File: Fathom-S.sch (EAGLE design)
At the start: 109 parts, among them IC1 LMH6643, IC2 LMH6643, IC3 ST490AB, IC4 ST490AB, IC5 FT230XS, Q1 BC817-40W, U1 MC7812, U2 MC7805, U4 INA139, U5 MC7805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

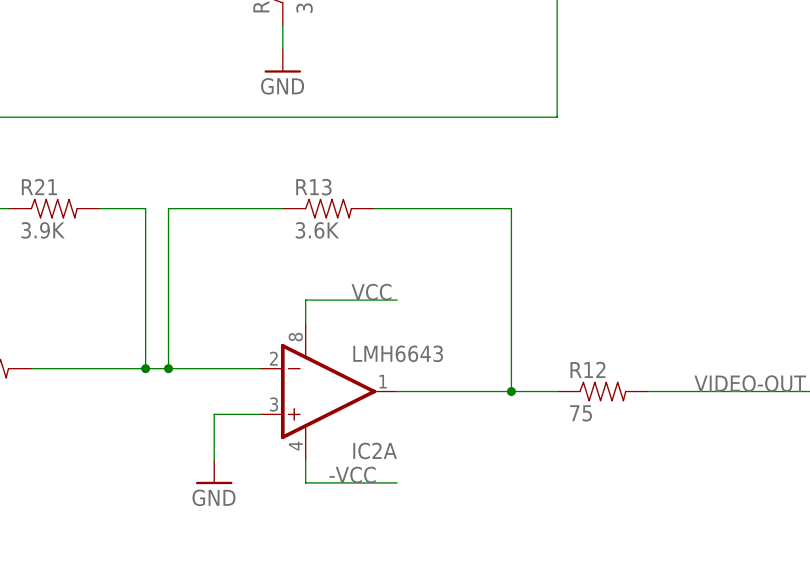
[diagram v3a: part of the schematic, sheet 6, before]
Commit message: Changed the op-amp package because the MSOPs are much cheaper for some reason.
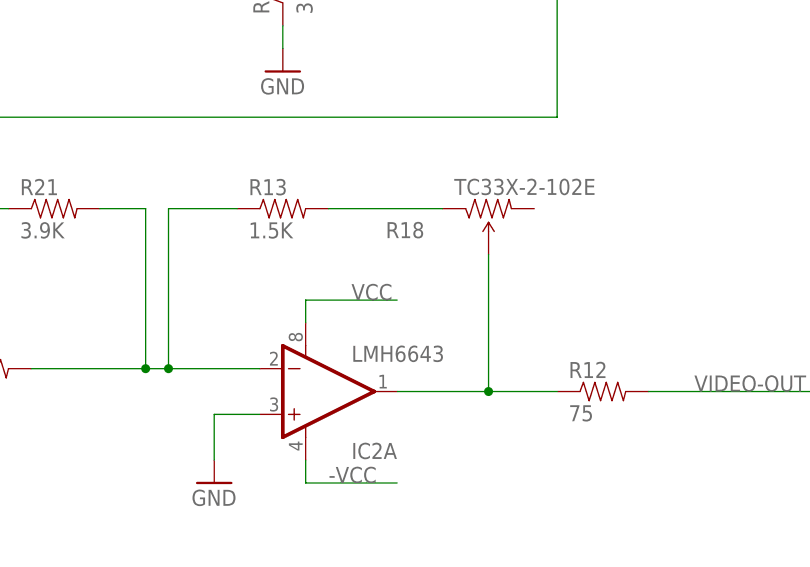
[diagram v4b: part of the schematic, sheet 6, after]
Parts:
- added R18: TC33X-2-102E, SparkFun-Electromechanical:TRIMPOT-2
- IC1, IC2: device SparkFun-AnalogIC:OPAMP-DUALU -> BlueRobotics-Main:OPAMP-DUALMSOP
- R13: value 3.6K -> 1.5K
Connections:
- new net N$12: R13.2, R18.CCW
- net N$17: now also R18.WIPER; no longer R13.2
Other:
- moved on the sheet: R13
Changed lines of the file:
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@@
 <grid distance="0.1" unitdist="inch" unit="inch" style="lines" multiple="1" display="no" altdistance="0.01" altunitdist="inch" altunit="inch"/>
 <layers>
-<layer number="1" name="Top" color="4" fill="1" visible="no" active="no"/>
-<layer number="2" name="Route2" color="1" fill="3" visible="no" active="no"/>
-<layer number="3" name="Route3" color="4" fill="3" visible="no" active="no"/>
-<layer number="14" name="Route14" color="1" fill="6" visible="no" active="no"/>
-<layer number="15" name="Route15" color="4" fill="6" visible="no" active="no"/>
-<layer number="16" name="Bottom" color="1" fill="1" visible="no" active="no"/>
-<layer number="17" name="Pads" color="2" fill="1" visible="no" active="no"/>
-<layer number="18" name="Vias" color="2" fill="1" visible="no" active="no"/>
-<layer number="19" name="Unrouted" color="6" fill="1" visible="no" active="no"/>
-<layer number="20" name="Dimension" color="15" fill="1" visible="no" active="no"/>
-<layer number="21" name="tPlace" color="7" fill="1" visible="no" active="no"/>
-<layer number="22" name="bPlace" color="7" fill="1" visible="no" active="no"/>
-<layer number="23" name="tOrigins" color="15" fill="1" visible="no" active="no"/>
-<layer number="24" name="bOrigins" color="15" fill="1" visible="no" active="no"/>
-<layer number="25" name="tNames" color="7" fill="1" visible="no" active="no"/>
-<layer number="26" name="bNames" color="7" fill="1" visible="no" active="no"/>
-<layer number="27" name="tValues" color="7" fill="1" visible="no" active="no"/>
-<layer number="28" name="bValues" color="7" fill="1" visible="no" active="no"/>
+<layer number="1" name="Top" color="4" fill="1" visible="yes" active="no"/>
+<layer number="2" name="Route2" color="1" fill="3" visible="yes" active="no"/>
+<layer number="3" name="Route3" color="4" fill="3" visible="yes" active="no"/>
+<layer number="14" name="Route14" color="1" fill="6" visible="yes" active="no"/>
+<layer number="15" name="Route15" color="4" fill="6" visible="yes" active="no"/>
+<layer number="16" name="Bottom" color="1" fill="1" visible="yes" active="no"/>
+<layer number="17" name="Pads" color="2" fill="1" visible="yes" active="no"/>
+<layer number="18" name="Vias" color="2" fill="1" visible="yes" active="no"/>
+<layer number="19" name="Unrouted" color="6" fill="1" visible="yes" active="no"/>
+<layer number="20" name="Dimension" color="15" fill="1" visible="yes" active="no"/>
+<layer number="21" name="tPlace" color="7" fill="1" visible="yes" active="no"/>
+<layer number="22" name="bPlace" color="7" fill="1" visible="yes" active="no"/>
+<layer number="23" name="tOrigins" color="15" fill="1" visible="yes" active="no"/>
+<layer number="24" name="bOrigins" color="15" fill="1" visible="yes" active="no"/>
+<layer number="25" name="tNames" color="7" fill="1" visible="yes" active="no"/>
+<layer number="26" name="bNames" color="7" fill="1" visible="yes" active="no"/>
+<layer number="27" name="tValues" color="7" fill="1" visible="yes" active="no"/>
+<layer number="28" name="bValues" color="7" fill="1" visible="yes" active="no"/>
 <layer number="29" name="tStop" color="7" fill="3" visible="no" active="no"/>
 <layer number="30" name="bStop" color="7" fill="6" visible="no" active="no"/>
@@
 <layer number="35" name="tGlue" color="7" fill="4" visible="no" active="no"/>
 <layer number="36" name="bGlue" color="7" fill="5" visible="no" active="no"/>
-<layer number="37" name="tTest" color="7" fill="1" visible="no" active="no"/>
-<layer number="38" name="bTest" color="7" fill="1" visible="no" active="no"/>
+<layer number="37" name="tTest" color="7" fill="1" visible="yes" active="no"/>
+<layer number="38" name="bTest" color="7" fill="1" visible="yes" active="no"/>
 <layer number="39" name="tKeepout" color="4" fill="11" visible="no" active="no"/>
 <layer number="40" name="bKeepout" color="1" fill="11" visible="no" active="no"/>
@@
 <layer number="44" name="Drills" color="7" fill="1" visible="no" active="no"/>
 <layer number="45" name="Holes" color="7" fill="1" visible="no" active="no"/>
-<layer number="46" name="Milling" color="3" fill="1" visible="no" active="no"/>
-<layer number="47" name="Measures" color="7" fill="1" visible="no" active="no"/>
-<layer number="48" name="Document" color="7" fill="1" visible="no" active="no"/>
-<layer number="49" name="Reference" color="7" fill="1" visible="no" active="no"/>
-<layer number="50" name="dxf" color="7" fill="1" visible="no" active="no"/>
-<layer number="51" name="tDocu" color="7" fill="1" visible="no" active="no"/>
-<layer number="52" name="bDocu" color="7" fill="1" visible="no" active="no"/>
-<layer number="53" name="tGND_GNDA" color="7" fill="9" visible="no" active="no"/>
-<layer number="54" name="bGND_GNDA" color="1" fill="9" visible="no" active="no"/>
-<layer number="56" name="wert" color="7" fill="1" visible="no" active="no"/>
-<layer number="57" name="tCAD" color="7" fill="1" visible="no" active="no"/>
+<layer number="46" name="Milling" color="3" fill="1" visible="yes" active="no"/>
+<layer number="47" name="Measures" color="7" fill="1" visible="yes" active="no"/>
+<layer number="48" name="Document" color="7" fill="1" visible="yes" active="no"/>
+<layer number="49" name="Reference" color="7" fill="1" visible="yes" active="no"/>
+<layer number="50" name="dxf" color="7" fill="1" visible="yes" active="no"/>
+<layer number="51" name="tDocu" color="7" fill="1" visible="yes" active="no"/>
+<layer number="52" name="bDocu" color="7" fill="1" visible="yes" active="no"/>
+<layer number="53" name="tGND_GNDA" color="7" fill="9" visible="yes" active="no"/>
+<layer number="54" name="bGND_GNDA" color="1" fill="9" visible="yes" active="no"/>
+<layer number="56" name="wert" color="7" fill="1" visible="yes" active="no"/>
+<layer number="57" name="tCAD" color="7" fill="1" visible="yes" active="no"/>
 <layer number="90" name="Modules" color="5" fill="1" visible="yes" active="yes"/>
 <layer number="91" name="Nets" color="2" fill="1" visible="yes" active="yes"/>
@@
 </classes>
 <parts>
-<part name="IC1" library="SparkFun-AnalogIC" deviceset="OPAMP-DUAL" device="U" value="LMH6643"/>
+<part name="IC1" library="BlueRobotics-Main" deviceset="OPAMP-DUAL" device="MSOP" value="LMH6643"/>
 <part name="R1" library="SparkFun-Passives" deviceset="RESISTOR" device="0603-RES" value="43"/>
 <part name="R2" library="SparkFun-Passives" deviceset="RESISTOR" device="0603-RES" value="3K"/>
@@
 <part name="C10" library="SparkFun-Passives" deviceset="CAP_POL" device="1206" value="10uF 16V"/>
 <part name="JP2" library="SparkFun-Connectors" deviceset="M08" device="3.5MM-8" value="3.5MM SCREW"/>
-<part name="IC2" library="SparkFun-AnalogIC" deviceset="OPAMP-DUAL" device="U" value="LMH6643"/>
+<part name="IC2" library="BlueRobotics-Main" deviceset="OPAMP-DUAL" device="MSOP" value="LMH6643"/>
 <part name="R8" library="SparkFun-Passives" deviceset="RESISTOR" device="0603-RES" value="3K"/>
 <part name="R9" library="SparkFun-Passives" deviceset="RESISTOR" device="0603-RES" value="3K"/>
@@
 <part name="R11" library="SparkFun-Passives" deviceset="RESISTOR" device="0603-RES" value="3K"/>
 <part name="R12" library="SparkFun-Passives" deviceset="RESISTOR" device="0603-RES" value="75"/>
-<part name="R13" library="SparkFun-Passives" deviceset="RESISTOR" device="0603-RES" value="3.6K"/>
+<part name="R13" library="SparkFun-Passives" deviceset="RESISTOR" device="0603-RES" value="1.5K"/>
 <part name="R14" library="SparkFun-Passives" deviceset="RESISTOR" device="0603-RES" value="86.6"/>
 <part name="GND8" library="SparkFun-Aesthetics" deviceset="GND" device=""/>
@@
 <part name="C26" library="SparkFun-Passives" deviceset="CAP" device="0805" value="10uF X5R 10V"/>
 <part name="C27" library="SparkFun-Passives" deviceset="CAP" device="0805" value="10uF X5R 10V"/>
+<part name="R18" library="SparkFun-Electromechanical" deviceset="TRIMPOT" device="-2" value="TC33X-2-102E"/>
 </parts>
 <sheets>
@@
 <instance part="R11" gate="G$1" x="180.34" y="121.92" rot="R90"/>
 <instance part="R12" gate="G$1" x="215.9" y="76.2"/>
-<instance part="R13" gate="G$1" x="185.42" y="96.52"/>
+<instance part="R13" gate="G$1" x="180.34" y="96.52"/>
 <instance part="R14" gate="G$1" x="154.94" y="134.62" rot="R90"/>
 <instance part="GND8" gate="1" x="172.72" y="66.04"/>
@@
 <instance part="R22" gate="G$1" x="147.32" y="78.74"/>
 <instance part="C17" gate="G$1" x="142.24" y="96.52" rot="R90"/>
+<instance part="R18" gate="R?" x="203.2" y="96.52" rot="MR180"/>
 </instances>
 <busses>
@@
 <junction x="167.64" y="78.74"/>
 <pinref part="R13" gate="G$1" pin="1"/>
-<wire x1="167.64" y1="96.52" x2="180.34" y2="96.52" width="0.1524" layer="91"/>
+<wire x1="167.64" y1="96.52" x2="175.26" y2="96.52" width="0.1524" layer="91"/>
 </segment>
 </net>
@@
 <net name="N$17" class="0">
 <segment>
-<pinref part="R13" gate="G$1" pin="2"/>
-<wire x1="190.5" y1="96.52" x2="205.74" y2="96.52" width="0.1524" layer="91"/>
-<wire x1="205.74" y1="96.52" x2="205.74" y2="76.2" width="0.1524" layer="91"/>
 <pinref part="IC2" gate="A" pin="OUT"/>
-<wire x1="205.74" y1="76.2" x2="193.04" y2="76.2" width="0.1524" layer="91"/>
 <pinref part="R12" gate="G$1" pin="1"/>
-<wire x1="210.82" y1="76.2" x2="205.74" y2="76.2" width="0.1524" layer="91"/>
-<junction x="205.74" y="76.2"/>
+<wire x1="210.82" y1="76.2" x2="203.2" y2="76.2" width="0.1524" layer="91"/>
+<pinref part="R18" gate="R?" pin="WIPER"/>
+<wire x1="203.2" y1="76.2" x2="193.04" y2="76.2" width="0.1524" layer="91"/>
+<wire x1="203.2" y1="91.44" x2="203.2" y2="76.2" width="0.1524" layer="91"/>
+<junction x="203.2" y="76.2"/>
 </segment>
 </net>
@@
 </segment>
 </net>
+<net name="N$12" class="0">
+<segment>
+<pinref part="R18" gate="R?" pin="CCW"/>
+<pinref part="R13" gate="G$1" pin="2"/>
+<wire x1="198.12" y1="96.52" x2="185.42" y2="96.52" width="0.1524" layer="91"/>
+</segment>
+</net>

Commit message: Minor changes to readme and silkscreen.
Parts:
- U$4: device BR-Eagle-Library:LOGOFULL-M -> BlueRobotics-Main:LOGOFULL-M
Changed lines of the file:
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@@
 <grid distance="0.1" unitdist="inch" unit="inch" style="lines" multiple="1" display="no" altdistance="0.01" altunitdist="inch" altunit="inch"/>
 <layers>
-<layer number="1" name="Top" color="4" fill="1" visible="yes" active="no"/>
-<layer number="2" name="Route2" color="1" fill="3" visible="yes" active="no"/>
-<layer number="3" name="Route3" color="4" fill="3" visible="yes" active="no"/>
-<layer number="14" name="Route14" color="1" fill="6" visible="yes" active="no"/>
-<layer number="15" name="Route15" color="4" fill="6" visible="yes" active="no"/>
-<layer number="16" name="Bottom" color="1" fill="1" visible="yes" active="no"/>
-<layer number="17" name="Pads" color="2" fill="1" visible="yes" active="no"/>
-<layer number="18" name="Vias" color="2" fill="1" visible="yes" active="no"/>
-<layer number="19" name="Unrouted" color="6" fill="1" visible="yes" active="no"/>
-<layer number="20" name="Dimension" color="15" fill="1" visible="yes" active="no"/>
-<layer number="21" name="tPlace" color="7" fill="1" visible="yes" active="no"/>
-<layer number="22" name="bPlace" color="7" fill="1" visible="yes" active="no"/>
-<layer number="23" name="tOrigins" color="15" fill="1" visible="yes" active="no"/>
-<layer number="24" name="bOrigins" color="15" fill="1" visible="yes" active="no"/>
-<layer number="25" name="tNames" color="7" fill="1" visible="yes" active="no"/>
-<layer number="26" name="bNames" color="7" fill="1" visible="yes" active="no"/>
-<layer number="27" name="tValues" color="7" fill="1" visible="yes" active="no"/>
-<layer number="28" name="bValues" color="7" fill="1" visible="yes" active="no"/>
+<layer number="1" name="Top" color="4" fill="1" visible="no" active="no"/>
+<layer number="2" name="Route2" color="1" fill="3" visible="no" active="no"/>
+<layer number="3" name="Route3" color="4" fill="3" visible="no" active="no"/>
+<layer number="14" name="Route14" color="1" fill="6" visible="no" active="no"/>
+<layer number="15" name="Route15" color="4" fill="6" visible="no" active="no"/>
+<layer number="16" name="Bottom" color="1" fill="1" visible="no" active="no"/>
+<layer number="17" name="Pads" color="2" fill="1" visible="no" active="no"/>
+<layer number="18" name="Vias" color="2" fill="1" visible="no" active="no"/>
+<layer number="19" name="Unrouted" color="6" fill="1" visible="no" active="no"/>
+<layer number="20" name="Dimension" color="15" fill="1" visible="no" active="no"/>
+<layer number="21" name="tPlace" color="7" fill="1" visible="no" active="no"/>
+<layer number="22" name="bPlace" color="7" fill="1" visible="no" active="no"/>
+<layer number="23" name="tOrigins" color="15" fill="1" visible="no" active="no"/>
+<layer number="24" name="bOrigins" color="15" fill="1" visible="no" active="no"/>
+<layer number="25" name="tNames" color="7" fill="1" visible="no" active="no"/>
+<layer number="26" name="bNames" color="7" fill="1" visible="no" active="no"/>
+<layer number="27" name="tValues" color="7" fill="1" visible="no" active="no"/>
+<layer number="28" name="bValues" color="7" fill="1" visible="no" active="no"/>
 <layer number="29" name="tStop" color="7" fill="3" visible="no" active="no"/>
 <layer number="30" name="bStop" color="7" fill="6" visible="no" active="no"/>
@@
 <layer number="35" name="tGlue" color="7" fill="4" visible="no" active="no"/>
 <layer number="36" name="bGlue" color="7" fill="5" visible="no" active="no"/>
-<layer number="37" name="tTest" color="7" fill="1" visible="yes" active="no"/>
-<layer number="38" name="bTest" color="7" fill="1" visible="yes" active="no"/>
+<layer number="37" name="tTest" color="7" fill="1" visible="no" active="no"/>
+<layer number="38" name="bTest" color="7" fill="1" visible="no" active="no"/>
 <layer number="39" name="tKeepout" color="4" fill="11" visible="no" active="no"/>
 <layer number="40" name="bKeepout" color="1" fill="11" visible="no" active="no"/>
@@
 <layer number="44" name="Drills" color="7" fill="1" visible="no" active="no"/>
 <layer number="45" name="Holes" color="7" fill="1" visible="no" active="no"/>
-<layer number="46" name="Milling" color="3" fill="1" visible="yes" active="no"/>
-<layer number="47" name="Measures" color="7" fill="1" visible="yes" active="no"/>
-<layer number="48" name="Document" color="7" fill="1" visible="yes" active="no"/>
-<layer number="49" name="Reference" color="7" fill="1" visible="yes" active="no"/>
-<layer number="50" name="dxf" color="7" fill="1" visible="yes" active="no"/>
-<layer number="51" name="tDocu" color="7" fill="1" visible="yes" active="no"/>
-<layer number="52" name="bDocu" color="7" fill="1" visible="yes" active="no"/>
-<layer number="53" name="tGND_GNDA" color="7" fill="9" visible="yes" active="no"/>
-<layer number="54" name="bGND_GNDA" color="1" fill="9" visible="yes" active="no"/>
-<layer number="56" name="wert" color="7" fill="1" visible="yes" active="no"/>
-<layer number="57" name="tCAD" color="7" fill="1" visible="yes" active="no"/>
+<layer number="46" name="Milling" color="3" fill="1" visible="no" active="no"/>
+<layer number="47" name="Measures" color="7" fill="1" visible="no" active="no"/>
+<layer number="48" name="Document" color="7" fill="1" visible="no" active="no"/>
+<layer number="49" name="Reference" color="7" fill="1" visible="no" active="no"/>
+<layer number="50" name="dxf" color="7" fill="1" visible="no" active="no"/>
+<layer number="51" name="tDocu" color="7" fill="1" visible="no" active="no"/>
+<layer number="52" name="bDocu" color="7" fill="1" visible="no" active="no"/>
+<layer number="53" name="tGND_GNDA" color="7" fill="9" visible="no" active="no"/>
+<layer number="54" name="bGND_GNDA" color="1" fill="9" visible="no" active="no"/>
+<layer number="56" name="wert" color="7" fill="1" visible="no" active="no"/>
+<layer number="57" name="tCAD" color="7" fill="1" visible="no" active="no"/>
 <layer number="90" name="Modules" color="5" fill="1" visible="yes" active="yes"/>
 <layer number="91" name="Nets" color="2" fill="1" visible="yes" active="yes"/>
@@
 <part name="STANDOFF8" library="SparkFun-Electromechanical" deviceset="STAND-OFF" device=""/>
 <part name="SJ2" library="SparkFun-Passives" deviceset="JUMPER-PAD-3-2OF3_NC_BY_PASTE" device="" value=""/>
-<part name="U$4" library="BR-Eagle-Library" deviceset="LOGO" device="FULL-M" value="LOGOFULL-M"/>
+<part name="U$4" library="BlueRobotics-Main" deviceset="LOGO" device="FULL-M" value="LOGOFULL-M"/>
 <part name="U$5" library="BR-Eagle-Library" deviceset="LOGO" device="BR-LOGO-MS" value="LOGOBR-LOGO-MS"/>
 <part name="JP15" library="SparkFun-Connectors" deviceset="M04" device="PTH" value="0.1&quot; HEADER"/>
